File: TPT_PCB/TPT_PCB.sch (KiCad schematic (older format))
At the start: 30 parts, among them J1 Conn_01x04, J2 Conn_01x04, J3 Conn_01x04, J4 Conn_01x04, J5 Conn_01x04, U1 TCA9548APWR, U2 STM32F103RCTx, Y1 32.768kHz, Y2 8MHz

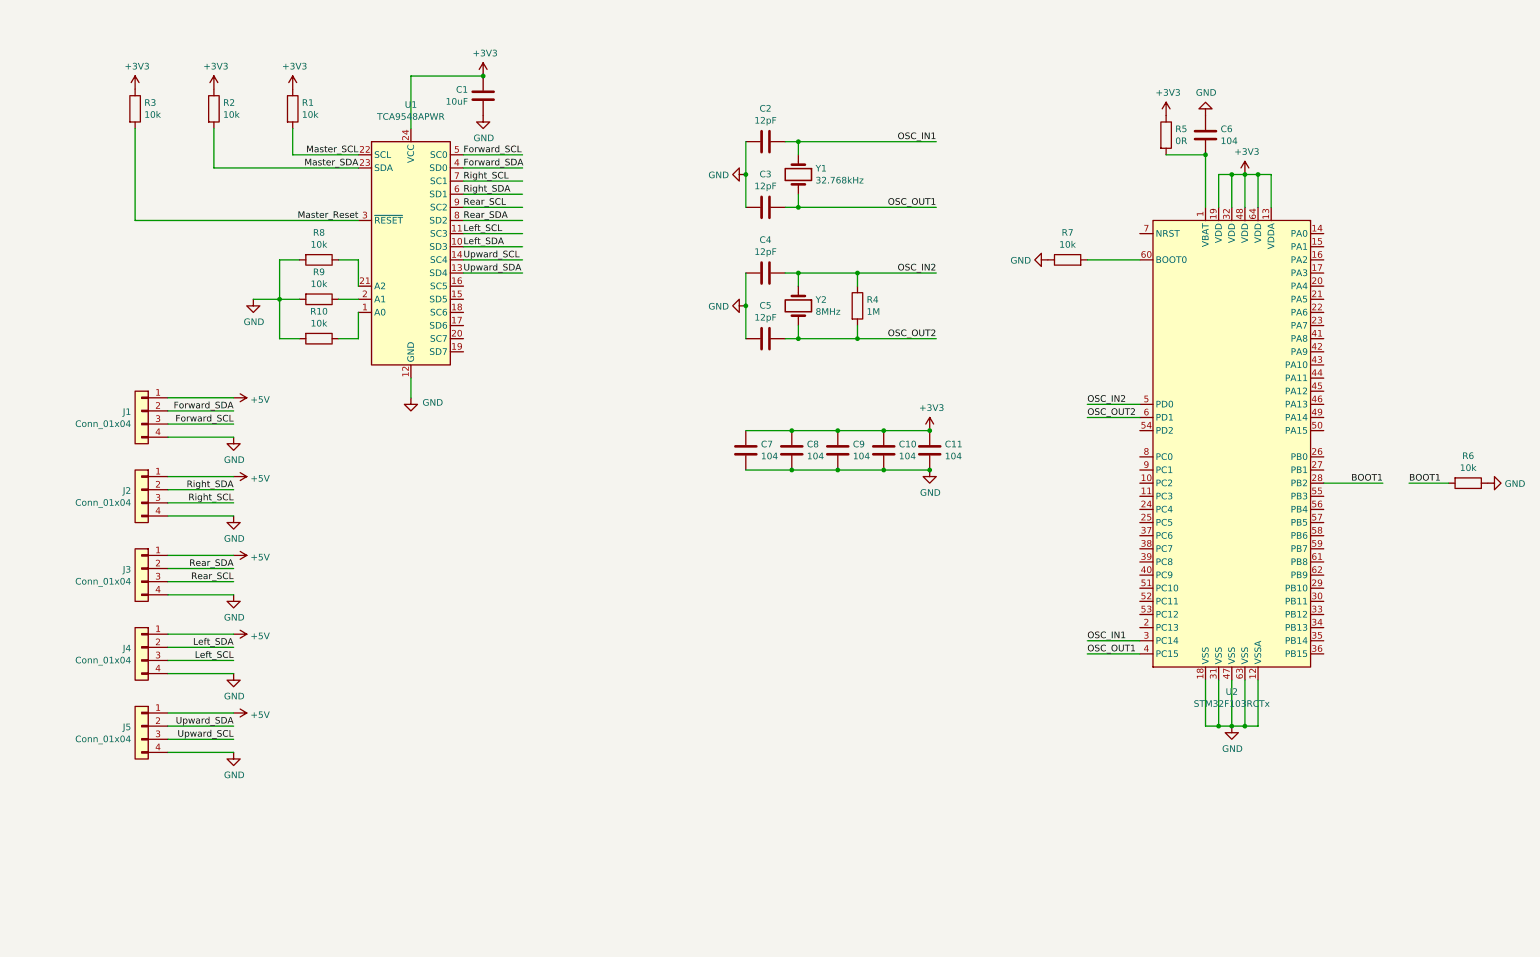
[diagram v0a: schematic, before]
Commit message: update pcb layout, but there are some problem. Must be re-do.
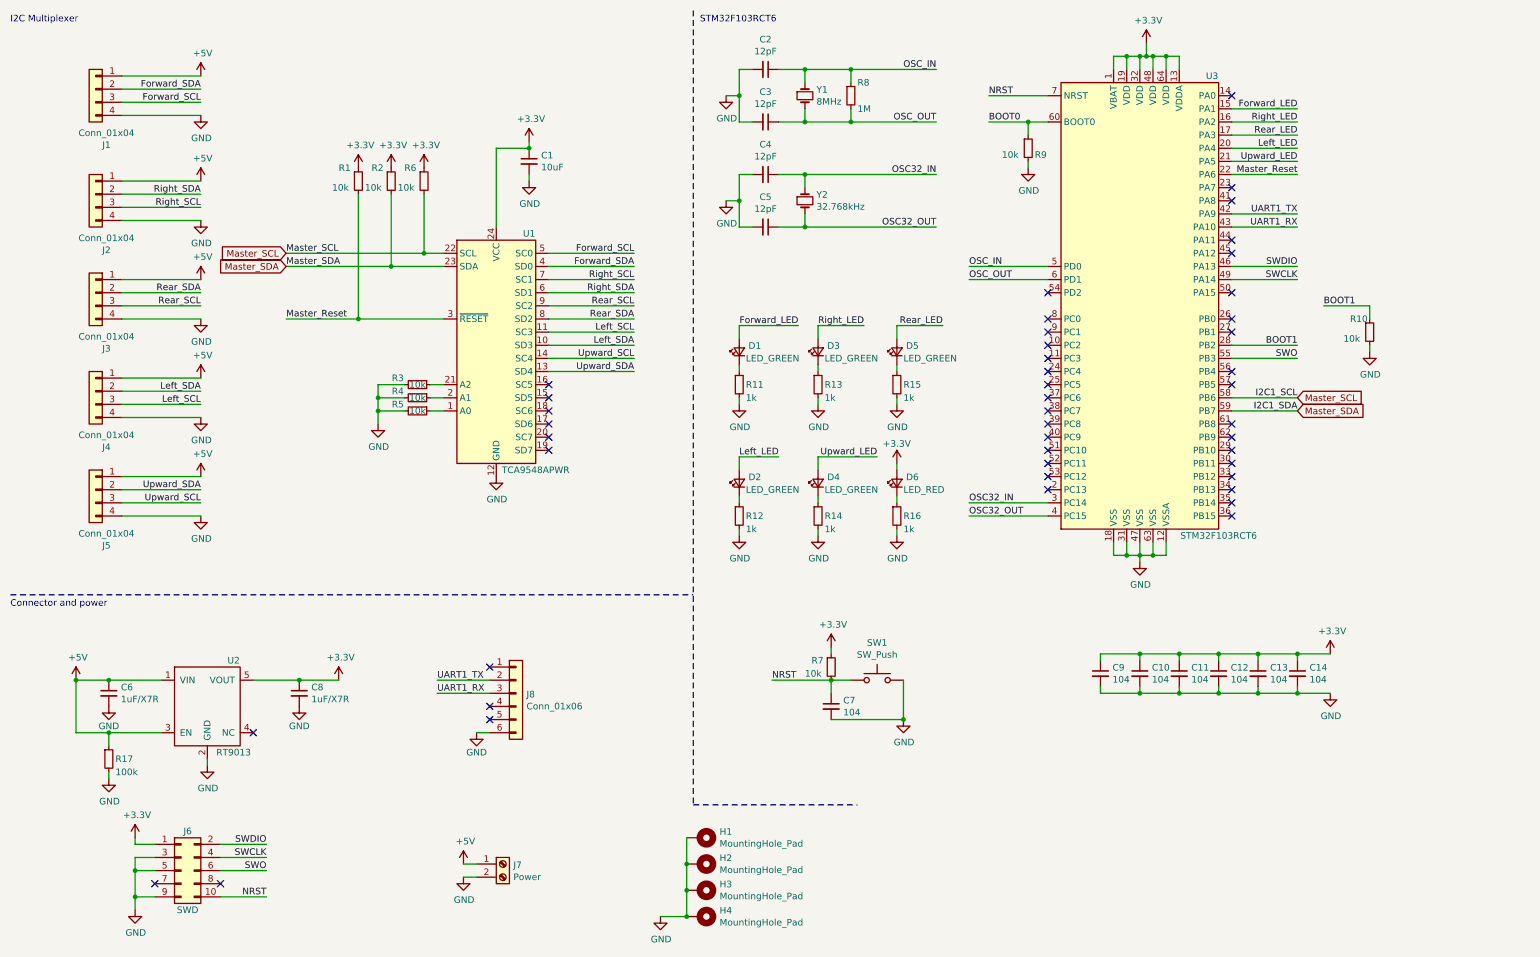
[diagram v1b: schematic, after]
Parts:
- removed C1: 10uF, Capacitor_SMD:C_0201_0603Metric_Pad0.64x0.40mm_HandSolder, symbol Device:C
- removed C10, C11, C6, C7, C8, C9: 104, symbol Device:C
- removed C2, C3, C4, C5: 12pF, symbol Device:C
- removed R1, R2, R3: 10k, Resistor_SMD:R_0201_0603Metric_Pad0.64x0.40mm_HandSolder, symbol Device:R
- removed R10, R6, R7, R8, R9: 10k, symbol Device:R
- removed R4: 1M, symbol Device:R
- removed R5: 0R, symbol Device:R
- removed U2: STM32F103RCTx, Package_QFP:LQFP-64_10x10mm_P0.5mm, symbol MCU_ST_STM32F1:STM32F103RCTx
- removed Y1: 32.768kHz, symbol Device:Crystal
- removed Y2: 8MHz, symbol Device:Crystal
- added C1: 10uF, Capacitor_SMD:C_0805_2012Metric, symbol Device:C_Small
- added C10, C11, C12, C13, C14, C7, C9: 104, Capacitor_SMD:C_0805_2012Metric, symbol Device:C_Small
- added C2, C3, C4, C5: 12pF, Capacitor_SMD:C_0805_2012Metric, symbol Device:C_Small
- added C6, C8: 1uF/X7R, Capacitor_SMD:C_0805_2012Metric, symbol Device:C_Small
- added D1, D2, D3, D4, D5: LED_GREEN, LED_SMD:LED_0805_2012Metric, symbol Device:LED_Small
- added D6: LED_RED, LED_SMD:LED_0805_2012Metric, symbol Device:LED_Small
- added H1, H2, H3, H4: MountingHole_Pad, MountingHole:MountingHole_4.3mm_M4_Pad_Via, symbol Mechanical:MountingHole_Pad
- added J6: SWD, Connector_PinSocket_1.27mm:PinSocket_2x05_P1.27mm_Vertical_SMD, symbol Connector_Generic:Conn_02x05_Odd_Even
- added J7: Power, TerminalBlock_Phoenix:TerminalBlock_Phoenix_PT-1,5-2-3.5-H_1x02_P3.50mm_Horizontal, symbol Connector:Screw_Terminal_01x02
- added J8: Conn_01x06, Connector_JST:JST_GH_SM06B-GHS-TB_1x06-1MP_P1.25mm_Horizontal, symbol Connector_Generic:Conn_01x06
- added R1, R10, R2, R3, R4, R5, R6, R7, R9: 10k, Resistor_SMD:R_0805_2012Metric, symbol Device:R_Small
- added R11, R12, R13, R14, R15, R16: 1k, Resistor_SMD:R_0805_2012Metric, symbol Device:R_Small
- added R17: 100k, Resistor_SMD:R_0805_2012Metric, symbol Device:R_Small
- added R8: 1M, Resistor_SMD:R_0805_2012Metric, symbol Device:R_Small
- added SW1: SW_Push, Button_Switch_SMD:SW_Push_1P1T_NO_6x6mm_H9.5mm, symbol Switch:SW_Push
- added U2: RT9013, Lizhou_Lib:SOT94P279X129-5N, symbol Lizhou_Lib:RT9013
- added U3: STM32F103RCT6, Package_QFP:LQFP-64_10x10mm_P0.5mm, symbol MCU_ST_STM32F1:STM32F103RCTx
- added Y1: 8MHz, Lizhou_Lib:XTAL_ABLS-8.000MHZ-B2-T, symbol Device:Crystal_Small
- added Y2: 32.768kHz, Lizhou_Lib:XTAL_AB26TRB-32.768KHZ-T, symbol Device:Crystal_Small
- J1, J2, J3, J4: footprint (none) -> Connector_JST:JST_GH_SM04B-GHS-TB_1x04-1MP_P1.25mm_Horizontal
- J5: footprint (none) -> Connector_JST:JST_GH_BM04B-GHS-TBT_1x04-1MP_P1.25mm_Vertical
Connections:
- net labels added: +3.3V, BOOT0, Forward_LED, I2C1_SCL, I2C1_SDA, Left_LED, NRST, OSC32_IN, OSC32_OUT, OSC_IN, OSC_OUT, Rear_LED, Right_LED, SWCLK, SWDIO, SWO, UART1_RX, UART1_TX, Upward_LED
- net labels removed: +3V3, OSC_IN1, OSC_IN2, OSC_OUT1, OSC_OUT2
- wire segments 105 -> 211
- no-connect marks 0 -> 45
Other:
- note added: "Connector and power"
- note added: "I2C Multiplexer"
- note added: "STM32F103RCT6"

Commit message: change SWD connector add layout TODO list
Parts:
- J6: footprint Connector_PinSocket_1.27mm:PinSocket_2x05_P1.27mm_Vertical_SMD -> Connector_Samtec_HLE_THT:Samtec_HLE-105-02-xx-DV-TE_2x05_P2.54mm_Horizontal
- U2: symbol Lizhou_Lib:RT9013 -> TPT_PCB-rescue:RT9013-Lizhou_Lib
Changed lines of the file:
@@
 BOOT1
 $Comp
-L Lizhou_Lib:RT9013 U2
+L TPT_PCB-rescue:RT9013-Lizhou_Lib U2
 U 1 1 6093BD8F
 P 2000 5800
@@
 F 0 "J6" H 1850 7350 50  0000 C CNN
 F 1 "SWD" H 1850 6750 50  0000 C CNN
-F 2 "Connector_PinSocket_1.27mm:PinSocket_2x05_P1.27mm_Vertical_SMD" H 1800 7050 50  0001 C CNN
+F 2 "Connector_Samtec_HLE_THT:Samtec_HLE-105-02-xx-DV-TE_2x05_P2.54mm_Horizontal" H 1800 7050 50  0001 C CNN
 F 3 "~" H 1800 7050 50  0001 C CNN
 	1    1800 7050
